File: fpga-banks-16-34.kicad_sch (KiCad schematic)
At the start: 24 parts, among them U3002 XC7K160T-FFG676, U9001 Oscillator_SMD_100MHz_ASFLMB, U9002 PCA9517A_TSSOP

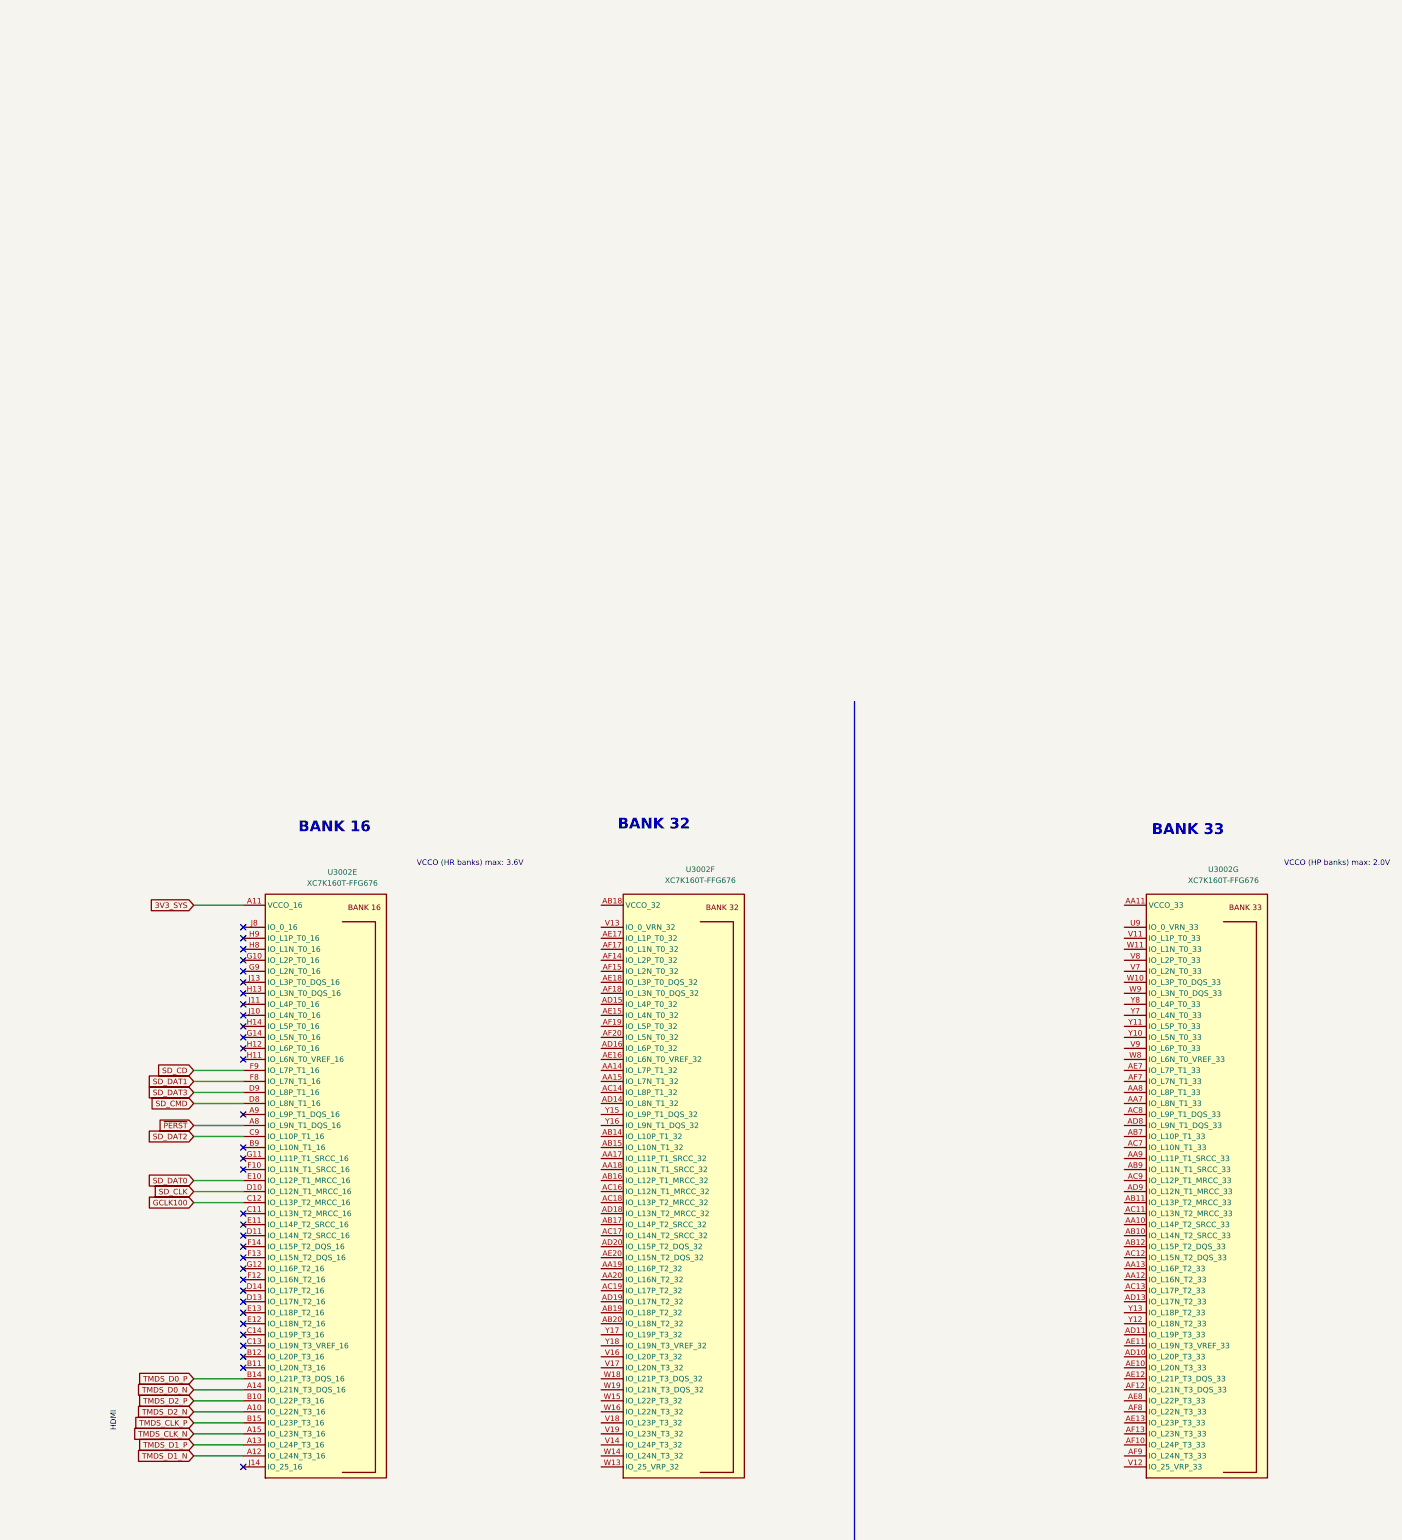
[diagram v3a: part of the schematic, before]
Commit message: Create pinout and fanout for FPGA bank 32
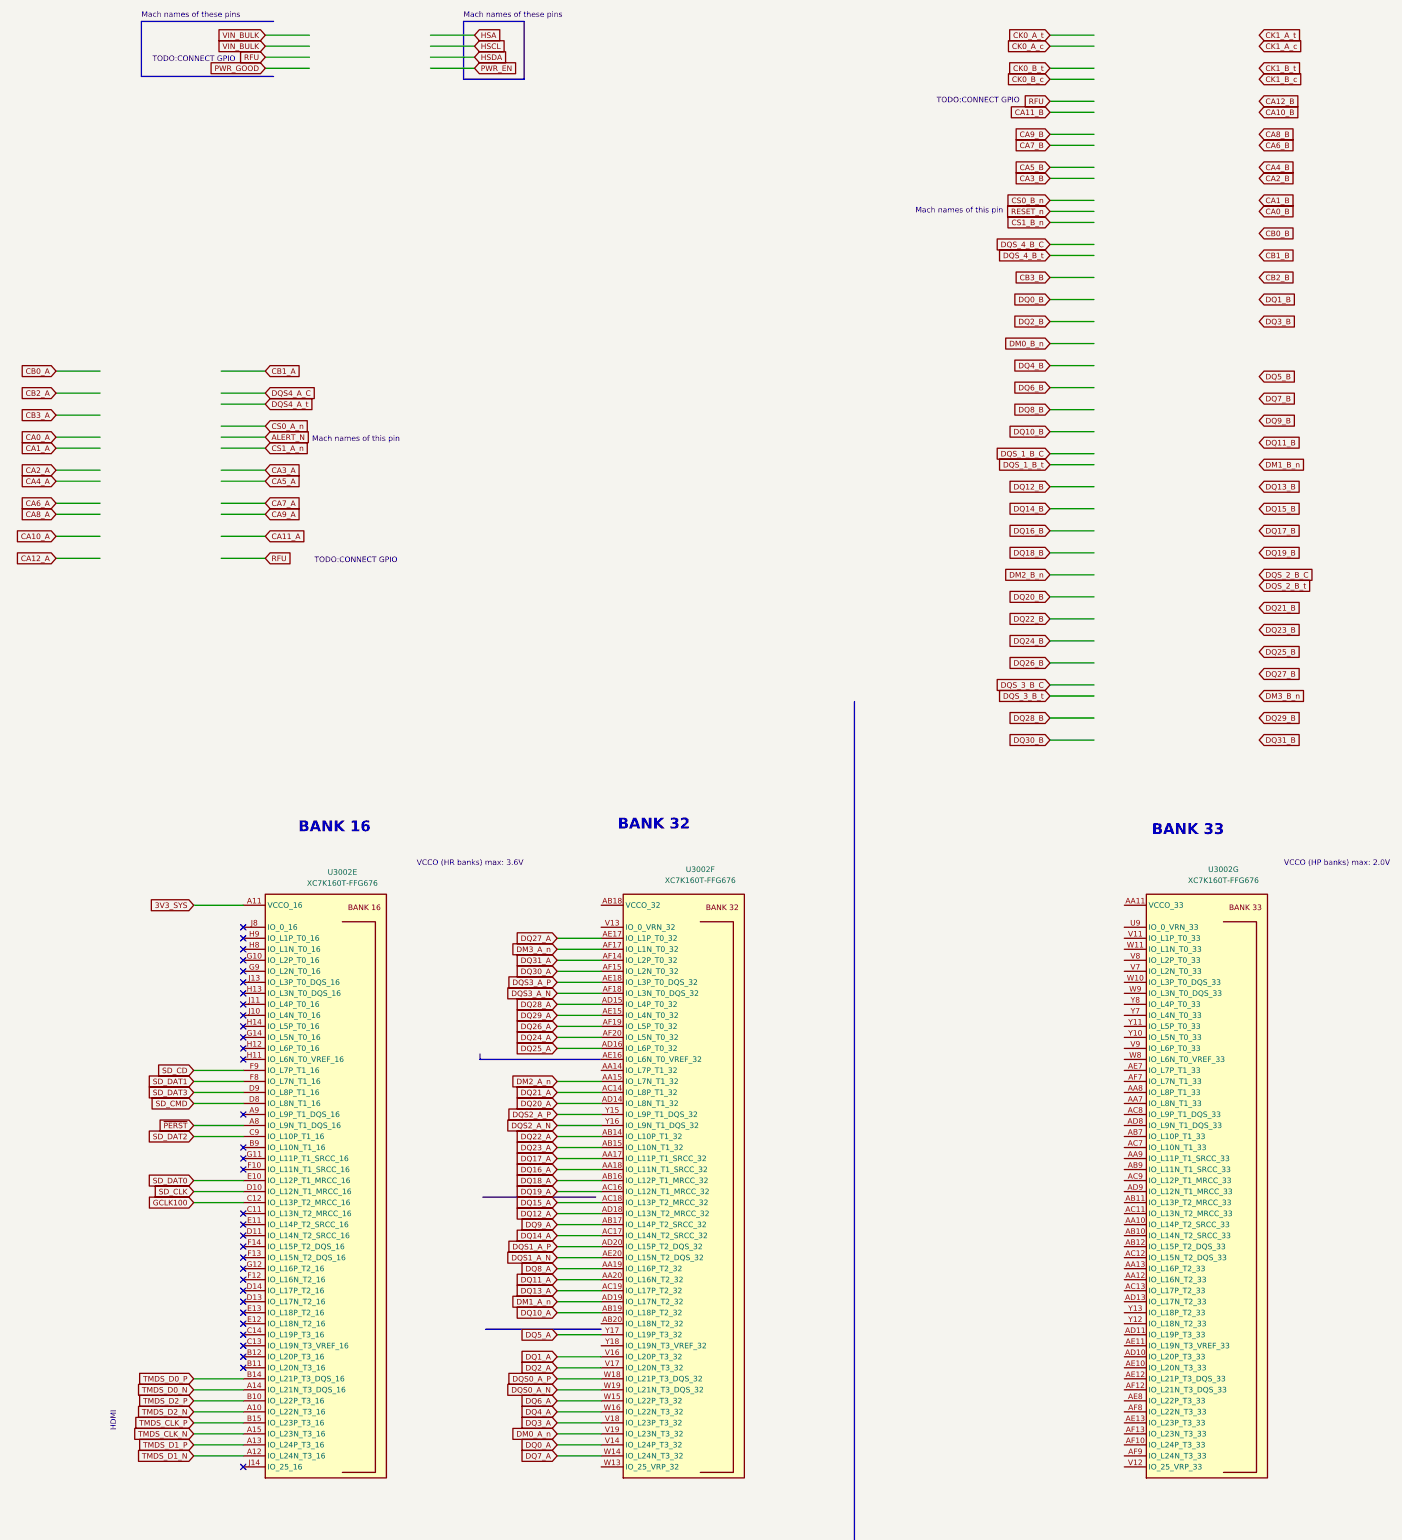
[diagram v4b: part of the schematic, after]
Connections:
- net DM2_A_n: now reaches U3002.AA15 (IO_L7N_T1_32)
- net DQ17_A: now reaches U3002.AA17 (IO_L11P_T1_SRCC_32)
- net DQ16_A: now reaches U3002.AA18 (IO_L11N_T1_SRCC_32)
- net DQ8_A: now reaches U3002.AA19 (IO_L16P_T2_32)
- net DQ11_A: now reaches U3002.AA20 (IO_L16N_T2_32)
- net DQ22_A: now reaches U3002.AB14 (IO_L10P_T1_32)
- net DQ23_A: now reaches U3002.AB15 (IO_L10N_T1_32)
- net DQ18_A: now reaches U3002.AB16 (IO_L12P_T1_MRCC_32)
- net DQ9_A: now reaches U3002.AB17 (IO_L14P_T2_SRCC_32)
- net DQ10_A: now reaches U3002.AB19 (IO_L18P_T2_32)
- net DQ21_A: now reaches U3002.AC14 (IO_L8P_T1_32)
- net DQ19_A: now reaches U3002.AC16 (IO_L12N_T1_MRCC_32)
- net DQ14_A: now reaches U3002.AC17 (IO_L14N_T2_SRCC_32)
- net DQ15_A: now reaches U3002.AC18 (IO_L13P_T2_MRCC_32)
- net DQ13_A: now reaches U3002.AC19 (IO_L17P_T2_32)
- net DQ20_A: now reaches U3002.AD14 (IO_L8N_T1_32)
- net DQ28_A: now reaches U3002.AD15 (IO_L4P_T0_32)
- net DQ25_A: now reaches U3002.AD16 (IO_L6P_T0_32)
- net DQ12_A: now reaches U3002.AD18 (IO_L13N_T2_MRCC_32)
- net DM1_A_n: now reaches U3002.AD19 (IO_L17N_T2_32)
- net DQS1_A_P: now reaches U3002.AD20 (IO_L15P_T2_DQS_32)
- net DQ29_A: now reaches U3002.AE15 (IO_L4N_T0_32)
- net DQ27_A: now reaches U3002.AE17 (IO_L1P_T0_32)
- net DQS3_A_P: now reaches U3002.AE18 (IO_L3P_T0_DQS_32)
- net DQS1_A_N: now reaches U3002.AE20 (IO_L15N_T2_DQS_32)
- net DQ31_A: now reaches U3002.AF14 (IO_L2P_T0_32)
- net DQ30_A: now reaches U3002.AF15 (IO_L2N_T0_32)
- net DM3_A_n: now reaches U3002.AF17 (IO_L1N_T0_32)
- net DQS3_A_N: now reaches U3002.AF18 (IO_L3N_T0_DQS_32)
- net DQ26_A: now reaches U3002.AF19 (IO_L5P_T0_32)
- net DQ24_A: now reaches U3002.AF20 (IO_L5N_T0_32)
- net DQ0_A: now reaches U3002.V14 (IO_L24P_T3_32)
- net DQ1_A: now reaches U3002.V16 (IO_L20P_T3_32)
- net DQ2_A: now reaches U3002.V17 (IO_L20N_T3_32)
- net DQ3_A: now reaches U3002.V18 (IO_L23P_T3_32)
- net DM0_A_n: now reaches U3002.V19 (IO_L23N_T3_32)
- net DQ7_A: now reaches U3002.W14 (IO_L24N_T3_32)
- net DQ6_A: now reaches U3002.W15 (IO_L22P_T3_32)
- net DQ4_A: now reaches U3002.W16 (IO_L22N_T3_32)
- net DQS0_A_P: now reaches U3002.W18 (IO_L21P_T3_DQS_32)
- net DQS0_A_N: now reaches U3002.W19 (IO_L21N_T3_DQS_32)
- net DQS2_A_P: now reaches U3002.Y15 (IO_L9P_T1_DQS_32)
- net DQS2_A_N: now reaches U3002.Y16 (IO_L9N_T1_DQS_32)
- net DQ5_A: now reaches U3002.Y17 (IO_L19P_T3_32)
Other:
- note added: "Mach names of these pins"
- note added: "Mach names of this pin"
- note added: "TODO:CONNECT GPIO"

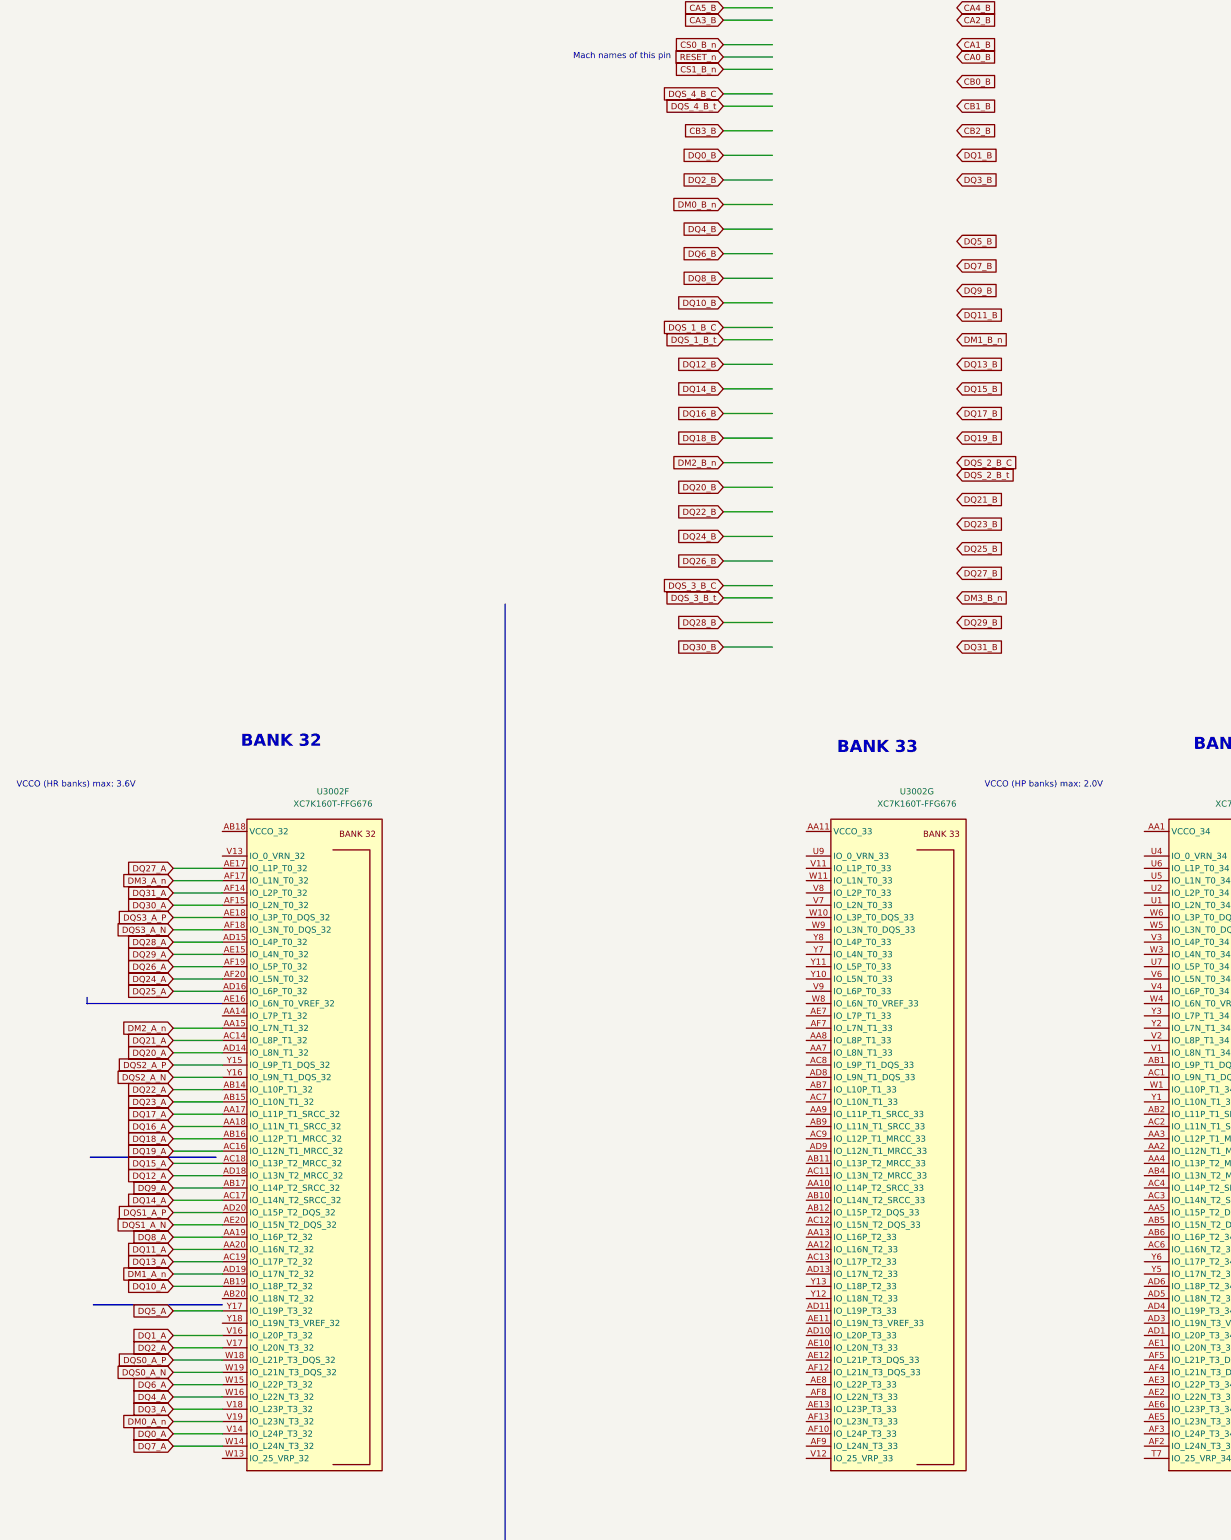
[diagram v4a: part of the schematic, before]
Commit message: Create pinout and fanout for FPGA bank 34
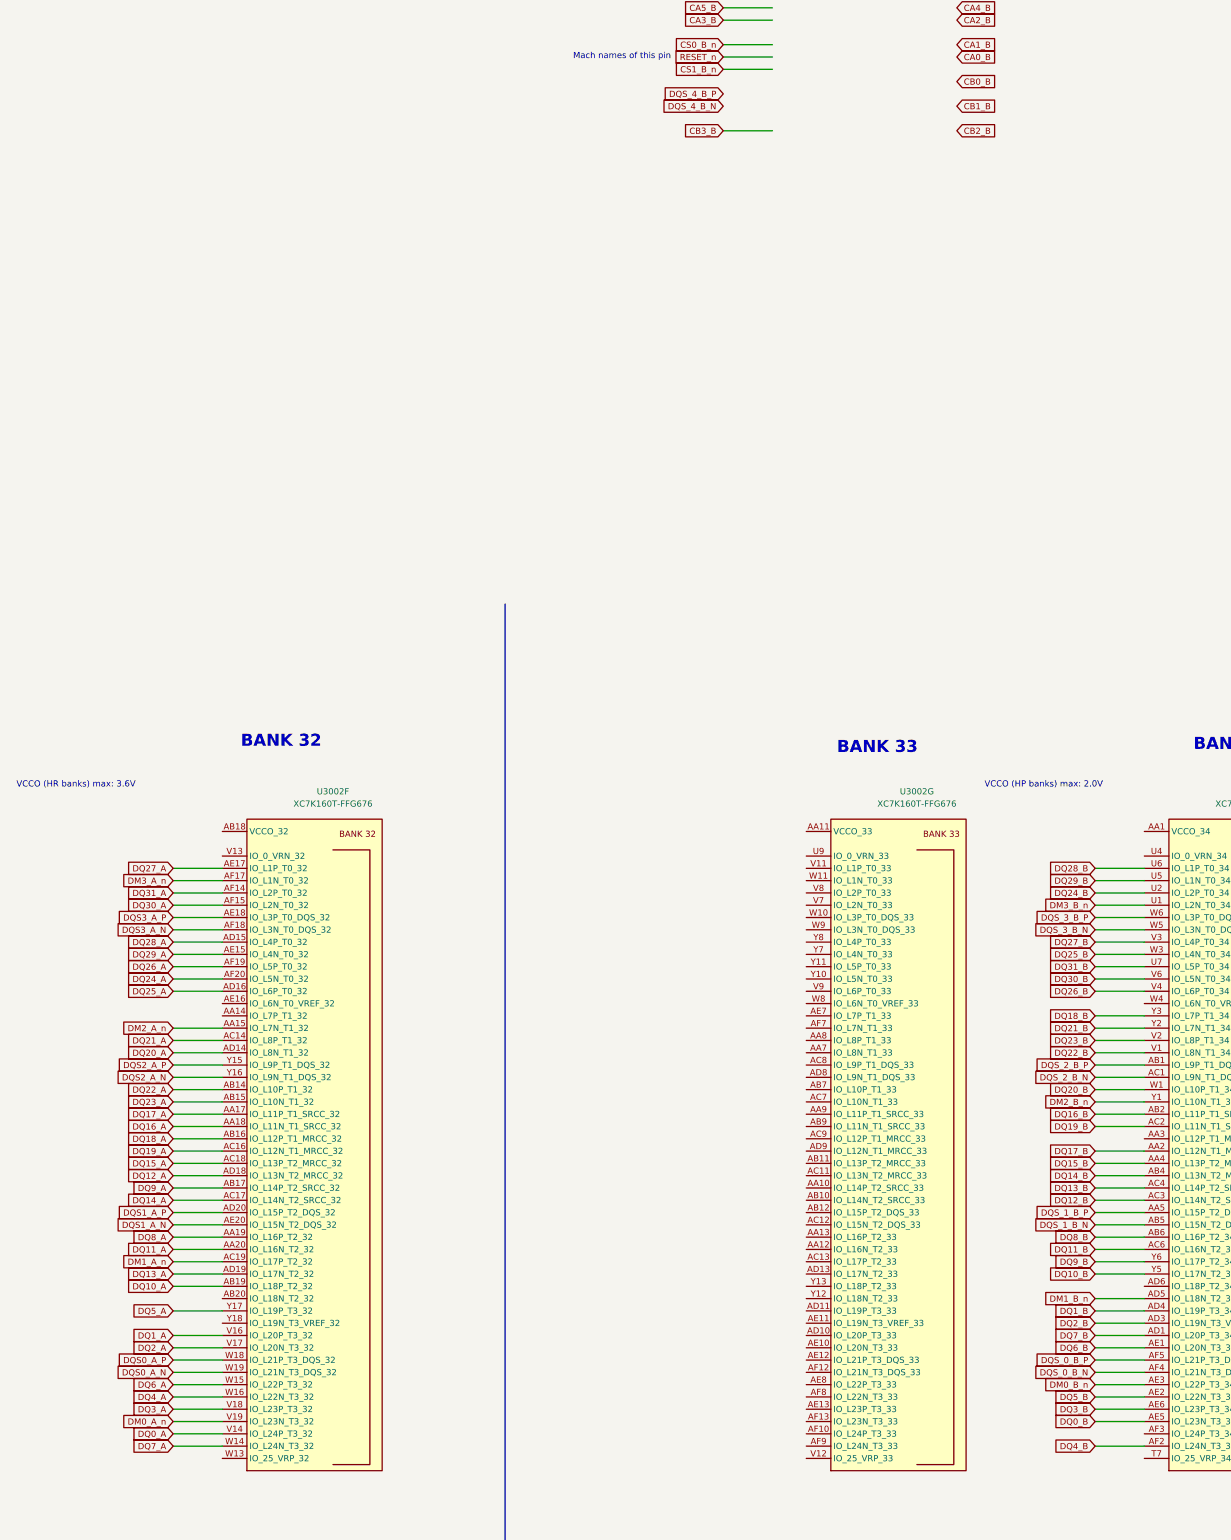
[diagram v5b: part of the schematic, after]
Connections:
- net DM0_B_n: now also U3002.AE3 (IO_L22P_T3_34)
- net DM1_A_n: now also U3002.AC19 (IO_L17P_T2_32); no longer U3002.AD19 (IO_L17N_T2_32)
- net DM1_B_n: now also U3002.AD5 (IO_L18N_T2_34)
- net DM2_B_n: now also U3002.Y1 (IO_L10N_T1_34)
- net DM3_B_n: now also U3002.U1 (IO_L2N_T0_34)
- net DQ0_B: now also U3002.AE5 (IO_L23N_T3_34)
- net DQ10_B: now also U3002.Y5 (IO_L17N_T2_34)
- net DQ11_B: now also U3002.AC6 (IO_L16N_T2_34)
- net DQ12_B: now also U3002.AC3 (IO_L14N_T2_SRCC_34)
- net DQ13_A: now also U3002.AD19 (IO_L17N_T2_32); no longer U3002.AC19 (IO_L17P_T2_32)
- net DQ13_B: now also U3002.AC4 (IO_L14P_T2_SRCC_34)
- net DQ14_B: now also U3002.AB4 (IO_L13N_T2_MRCC_34)
- net DQ15_B: now also U3002.AA4 (IO_L13P_T2_MRCC_34)
- net DQ16_B: now also U3002.AB2 (IO_L11P_T1_SRCC_34)
- net DQ17_B: now also U3002.AA2 (IO_L12N_T1_MRCC_34)
- net DQ18_B: now also U3002.Y3 (IO_L7P_T1_34)
- net DQ19_B: now also U3002.AC2 (IO_L11N_T1_SRCC_34)
- net DQ1_B: now also U3002.AD4 (IO_L19P_T3_34)
- net DQ20_B: now also U3002.W1 (IO_L10P_T1_34)
- net DQ21_B: now also U3002.Y2 (IO_L7N_T1_34)
- net DQ22_B: now also U3002.V1 (IO_L8N_T1_34)
- net DQ23_B: now also U3002.V2 (IO_L8P_T1_34)
- net DQ24_B: now also U3002.U2 (IO_L2P_T0_34)
- net DQ25_B: now also U3002.W3 (IO_L4N_T0_34)
- net DQ26_B: now also U3002.V4 (IO_L6P_T0_34)
- net DQ27_B: now also U3002.V3 (IO_L4P_T0_34)
- net DQ28_B: now also U3002.U6 (IO_L1P_T0_34)
- net DQ29_B: now also U3002.U5 (IO_L1N_T0_34)
- net DQ2_B: now also U3002.AD3 (IO_L19N_T3_VREF_34)
- net DQ30_B: now also U3002.V6 (IO_L5N_T0_34)
- net DQ31_B: now also U3002.U7 (IO_L5P_T0_34)
- net DQ3_B: now also U3002.AE6 (IO_L23P_T3_34)
- net DQ4_B: now also U3002.AF2 (IO_L24N_T3_34)
- net DQ5_B: now also U3002.AE2 (IO_L22N_T3_34)
- net DQ6_B: now also U3002.AE1 (IO_L20N_T3_34)
- net DQ7_B: now also U3002.AD1 (IO_L20P_T3_34)
- net DQ8_B: now also U3002.AB6 (IO_L16P_T2_34)
- net DQ9_B: now also U3002.Y6 (IO_L17P_T2_34)
- net DQS_1_B_P: now reaches U3002.AA5 (IO_L15P_T2_DQS_34)
- net DQS_2_B_P: now reaches U3002.AB1 (IO_L9P_T1_DQS_34)
- net DQS_1_B_N: now reaches U3002.AB5 (IO_L15N_T2_DQS_34)
- net DQS_2_B_N: now reaches U3002.AC1 (IO_L9N_T1_DQS_34)
- net DQS_0_B_N: now reaches U3002.AF4 (IO_L21N_T3_DQS_34)
- net DQS_0_B_P: now reaches U3002.AF5 (IO_L21P_T3_DQS_34)
- net DQS_3_B_N: now reaches U3002.W5 (IO_L3N_T0_DQS_34)
- net DQS_3_B_P: now reaches U3002.W6 (IO_L3P_T0_DQS_34)
